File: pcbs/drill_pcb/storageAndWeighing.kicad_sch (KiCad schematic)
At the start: 34 parts, among them J401 Screw_Terminal_01x04, J402 Screw_Terminal_01x06, J403 Screw_Terminal_01x04, SW401 SW_Push, SW402 SW_Push, SW403 SW_Push, U401 HT75xx-1-SOT89

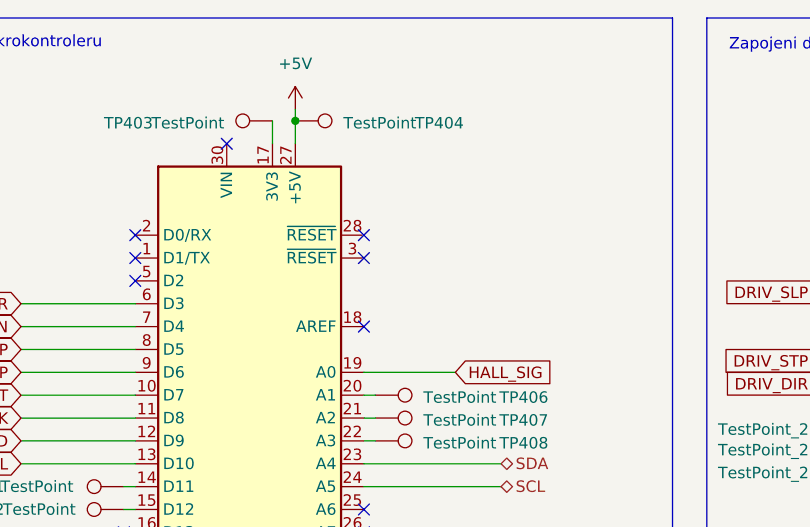
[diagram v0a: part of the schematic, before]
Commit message: added RESET connections into subsheets
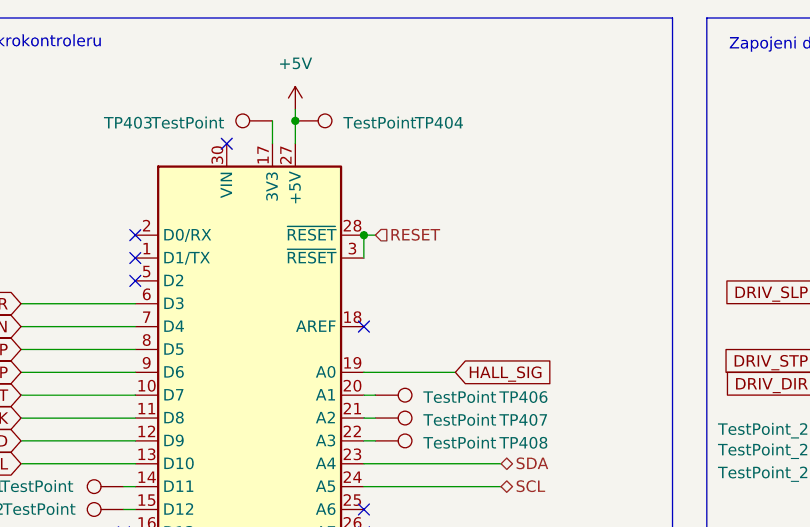
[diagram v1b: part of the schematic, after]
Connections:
- net RESET: now reaches A401.28 (~{RESET})
- net RESET: now also A401.3 (~{RESET})
- no-connect marks 11 -> 9
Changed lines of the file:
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@@
+	)
+	(junction
+		(at 68.58 39.37)
+		(diameter 0)
+		(color 0 0 0 0)
 	)
 	(junction
@@
 	)
 	(no_connect
-		(at 68.58 39.37)
-	)
-	(no_connect
 		(at 41.91 72.39)
 	)
@@
 	)
 	(no_connect
-		(at 68.58 41.91)
-	)
-	(no_connect
 		(at 68.58 72.39)
 	)
@@
 	(wire
 		(pts
+			(xy 68.58 39.37) (xy 69.85 39.37)
+		)
+		(stroke
+			(width 0)
+			(type default)
+		)
+	)
+	(wire
+		(pts
 			(xy 248.92 25.4) (xy 259.08 25.4)
 		)
@@
 		(pts
 			(xy 162.56 120.65) (xy 153.67 120.65)
+		)
+		(stroke
+			(width 0)
+			(type default)
+		)
+	)
+	(wire
+		(pts
+			(xy 68.58 39.37) (xy 68.58 41.91)
 		)
 		(stroke
@@
 		(fields_autoplaced yes)
 		(effects
+			(font
+				(size 1.27 1.27)
+			)
+			(justify left)
+		)
+	)
+	(hierarchical_label "RESET"
+		(shape input)
+		(at 69.85 39.37 0)
+		(fields_autoplaced yes)
+		(effects

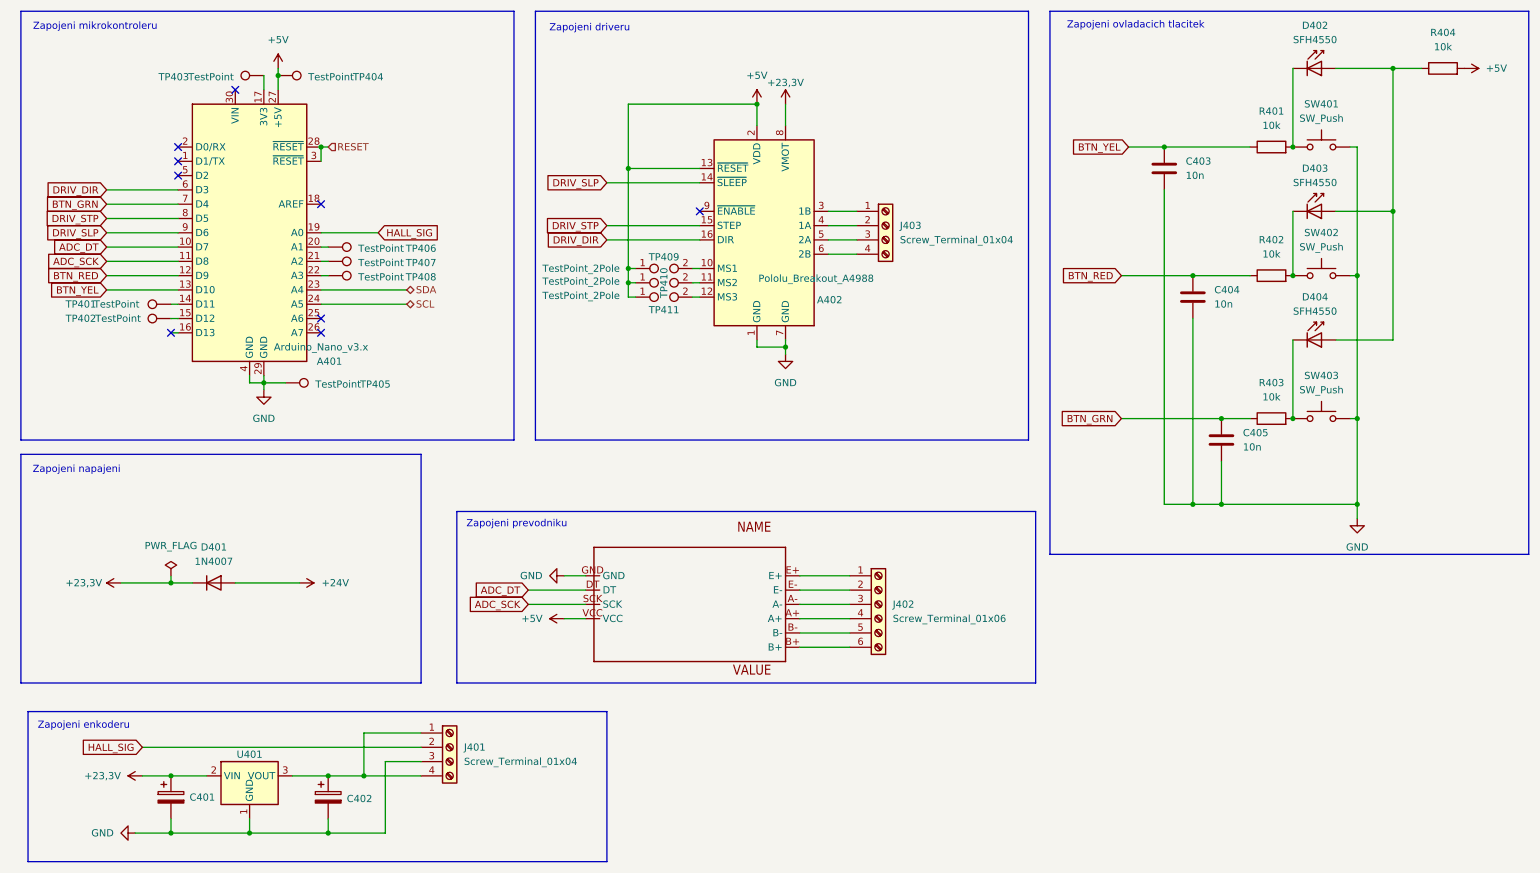
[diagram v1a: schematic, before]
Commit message: Mostly finished PCB v1.0.0 Missing strain gauge control circuit
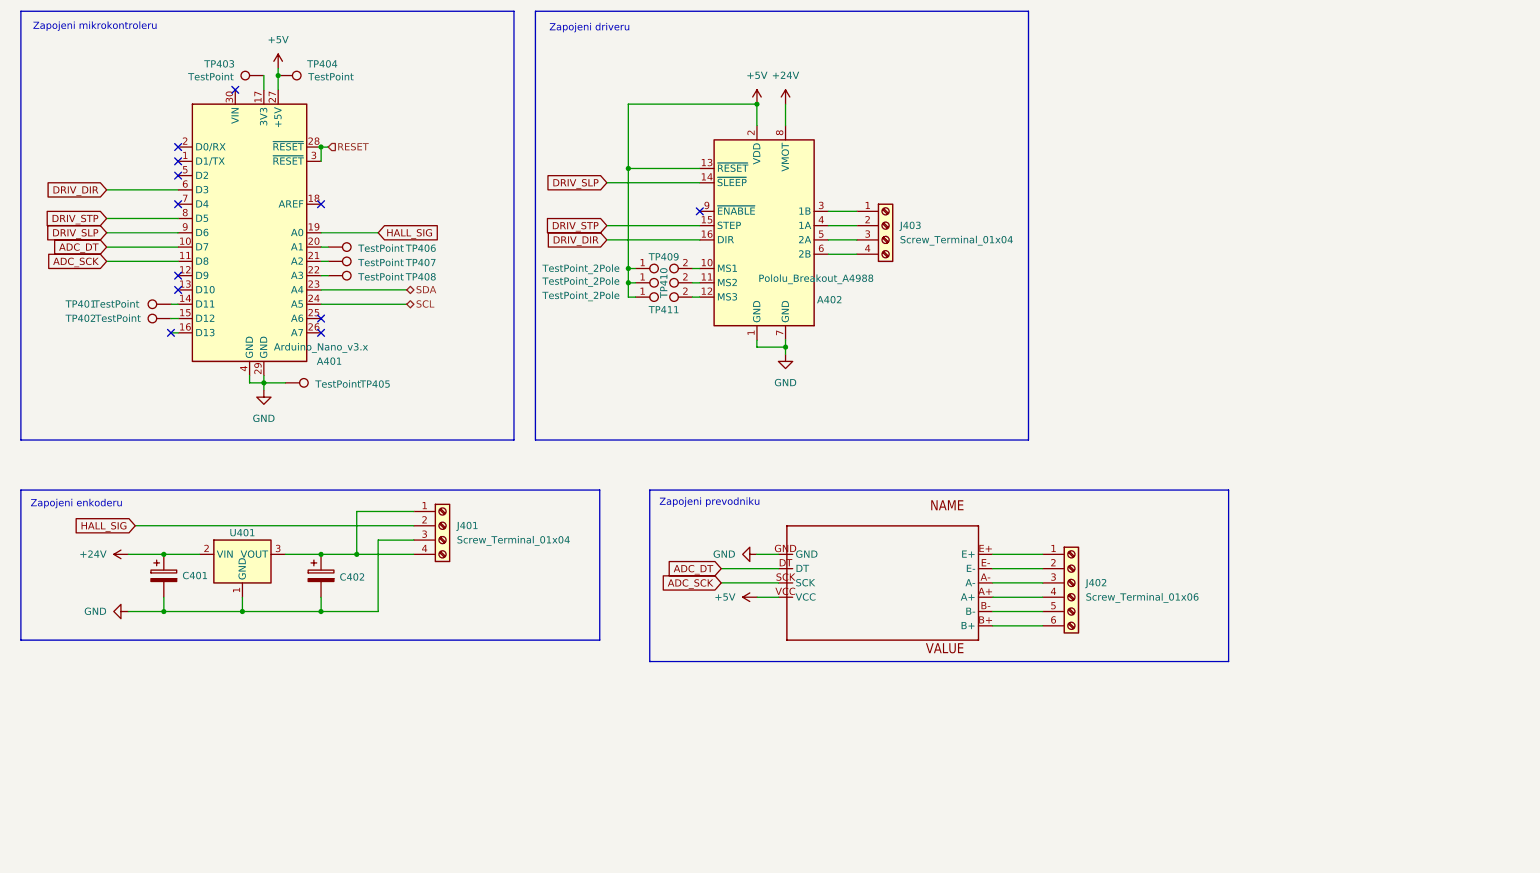
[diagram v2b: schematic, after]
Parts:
- removed C403, C404, C405: 10n, Capacitor_THT:C_Disc_D4.7mm_W2.5mm_P5.00mm, symbol Device:C
- removed D401: 1N4007, Diode_THT:D_DO-41_SOD81_P10.16mm_Horizontal, symbol Diode:1N4007
- removed D402, D403, D404: SFH4550, LED_THT:LED_D5.0mm_IRGrey, symbol LED:SFH4550
- removed R401, R402, R403, R404: 10k, Resistor_THT:R_Axial_DIN0207_L6.3mm_D2.5mm_P10.16mm_Horizontal, symbol Device:R
- removed SW401, SW402, SW403: SW_Push, Button_Switch_THT:SW_PUSH_6mm, symbol Switch:SW_Push
- J401, J403: footprint TerminalBlock_TE-Connectivity:TerminalBlock_TE_282834-4_1x04_P2.54mm_Horizontal -> Connector_JST:JST_XH_B4B-XH-A_1x04_P2.50mm_Vertical
- J402: footprint TerminalBlock_TE-Connectivity:TerminalBlock_TE_282834-6_1x06_P2.54mm_Horizontal -> Connector_JST:JST_XH_B6B-XH-A_1x06_P2.50mm_Vertical
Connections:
- net +23,3V is gone; now on net +24V: A402.8 (VMOT), C401.1, U401.2 (VIN)
- net BTN_GRN: no longer names the net of A401.7 (D4)
- net BTN_RED: no longer names the net of A401.12 (D9)
- net BTN_YEL: no longer names the net of A401.13 (D10)
- no-connect marks 9 -> 12
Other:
- note removed: "Zapojeni napajeni"
- note removed: "Zapojeni ovladacich tlacitek"
- moved on the sheet: C401, C402, J401, J402, U401

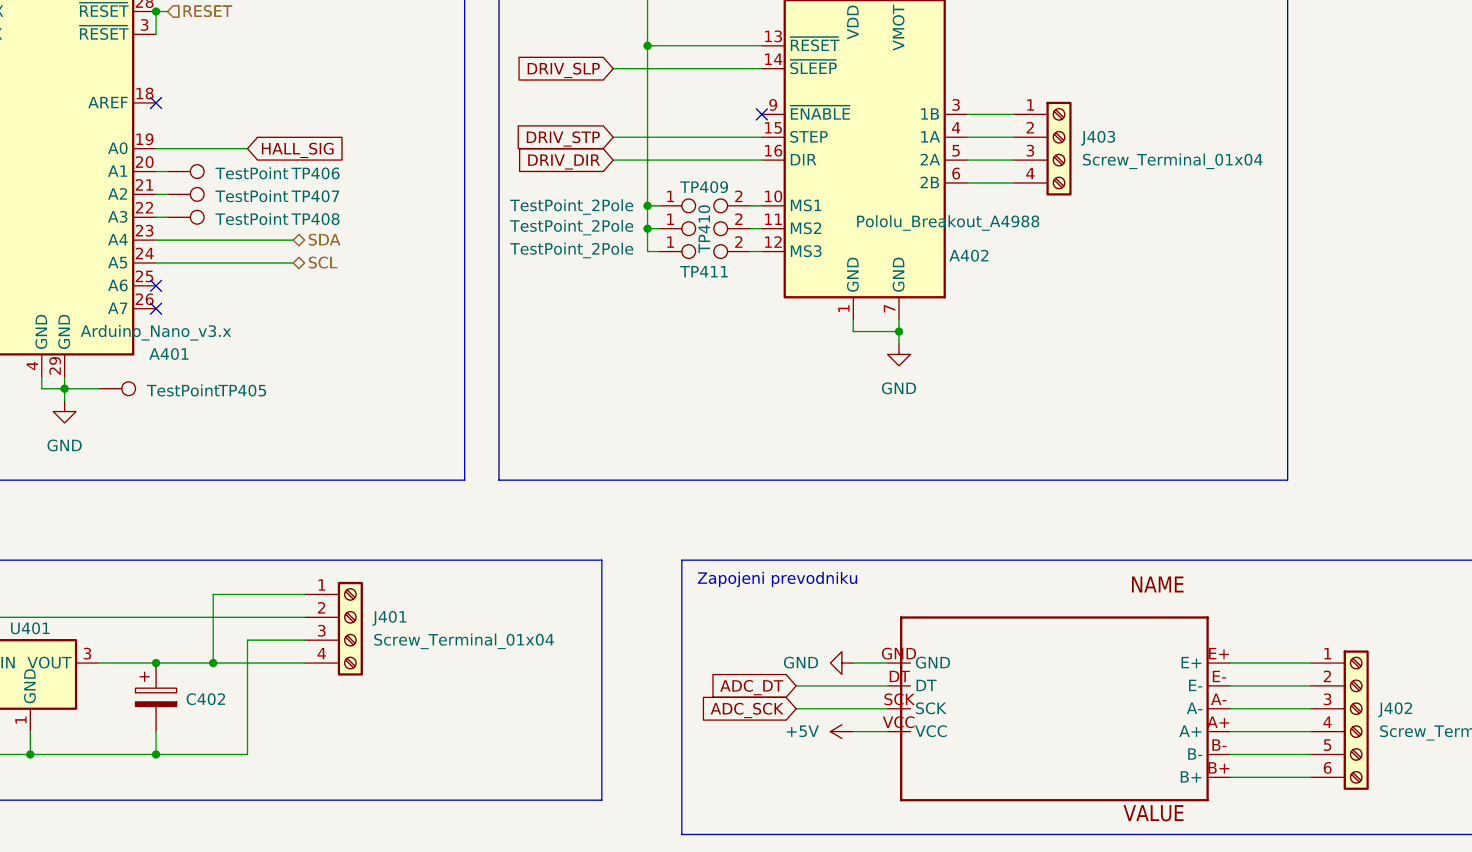
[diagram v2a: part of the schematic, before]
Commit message: update pouzdra konvertoru
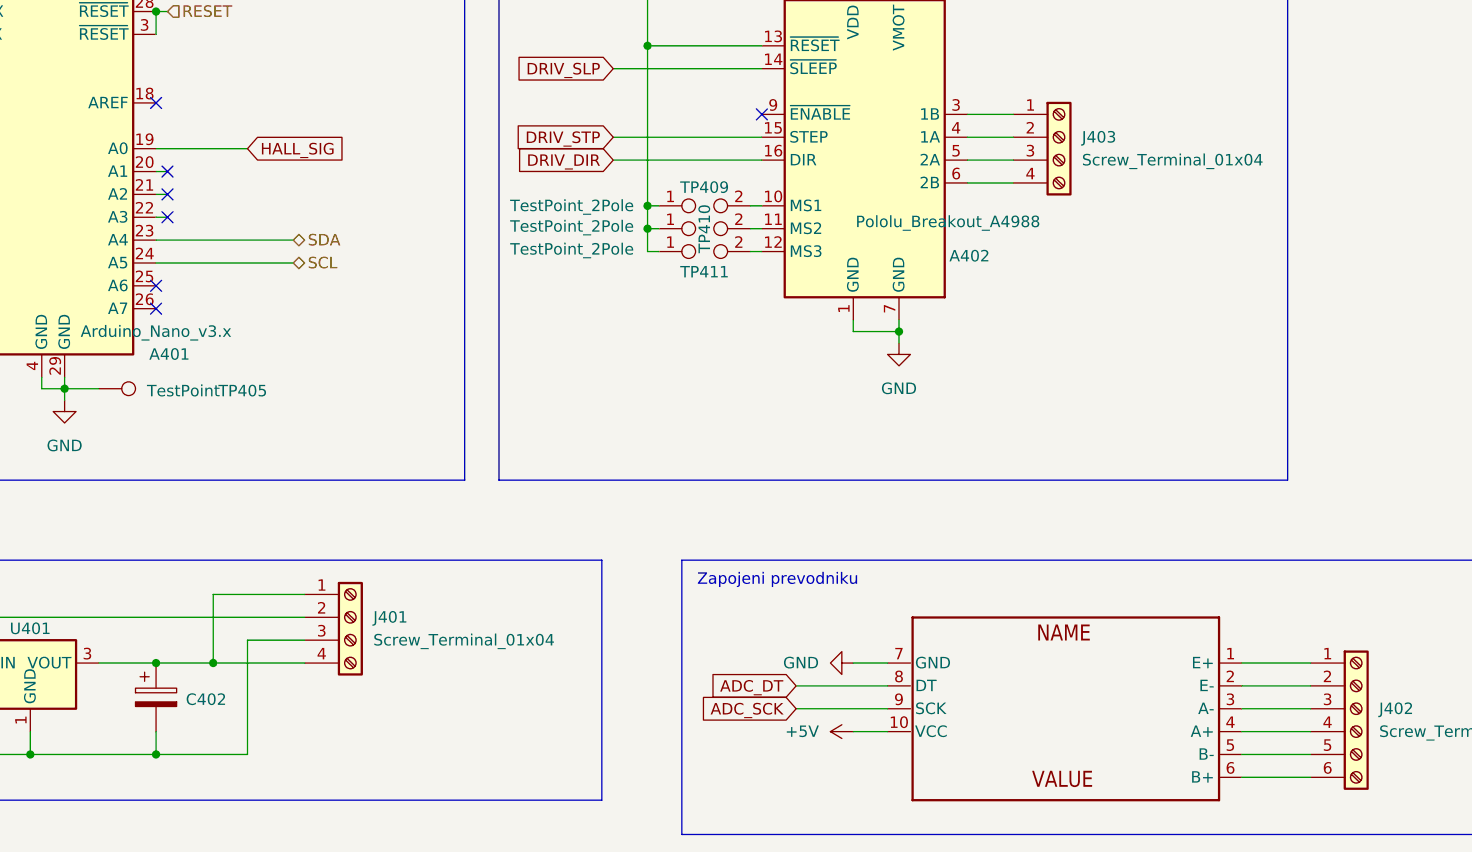
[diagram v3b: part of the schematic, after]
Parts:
- removed TP406, TP407, TP408: TestPoint, TestPoint:TestPoint_Pad_1.5x1.5mm, symbol Connector:TestPoint
- 1111401: footprint hx711footp:HX711 -> drill_hx711footp:HX711
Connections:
- net +5V: now also 1111401.10 (VCC); no longer 1111401.VCC
- net ADC_DT: now also 1111401.8 (DT); no longer 1111401.DT
- net ADC_SCK: now also 1111401.9 (SCK); no longer 1111401.SCK
- net GND: now also 1111401.7 (GND); no longer 1111401.GND
- net at J402.4 (Pin_4): now also 1111401.4 (A+); no longer 1111401.A+
- net at J402.3 (Pin_3): now also 1111401.3 (A-); no longer 1111401.A-
- net at J402.6 (Pin_6): now also 1111401.6 (B+); no longer 1111401.B+
- net at J402.5 (Pin_5): now also 1111401.5 (B-); no longer 1111401.B-
- net at J402.1 (Pin_1): now also 1111401.1 (E+); no longer 1111401.E+
- net at J402.2 (Pin_2): now also 1111401.2 (E-); no longer 1111401.E-
- no-connect marks 12 -> 15

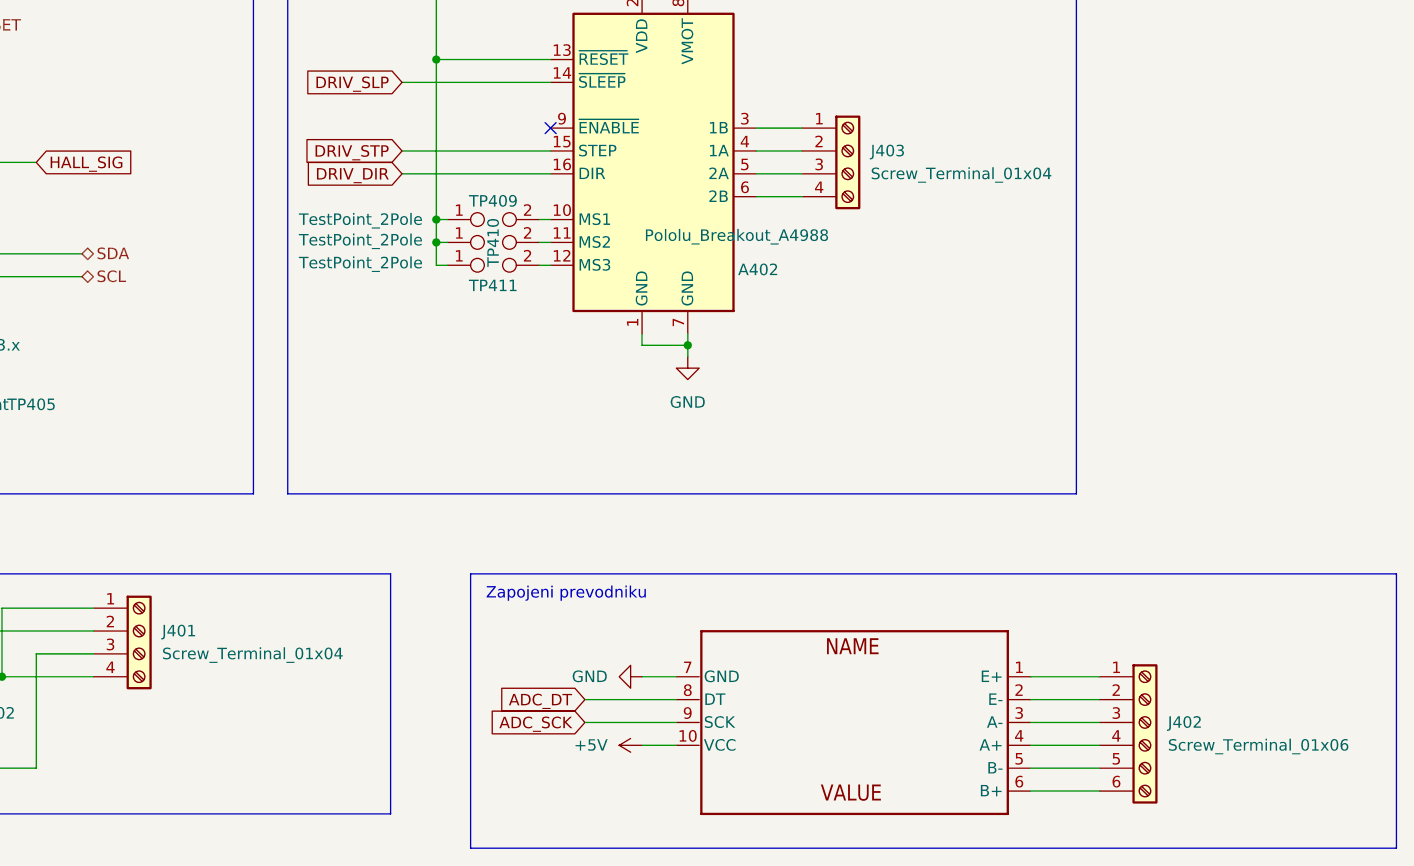
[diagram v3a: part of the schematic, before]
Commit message: PCB update Fixed connector silkscreen. Added H-bridge capacitors.
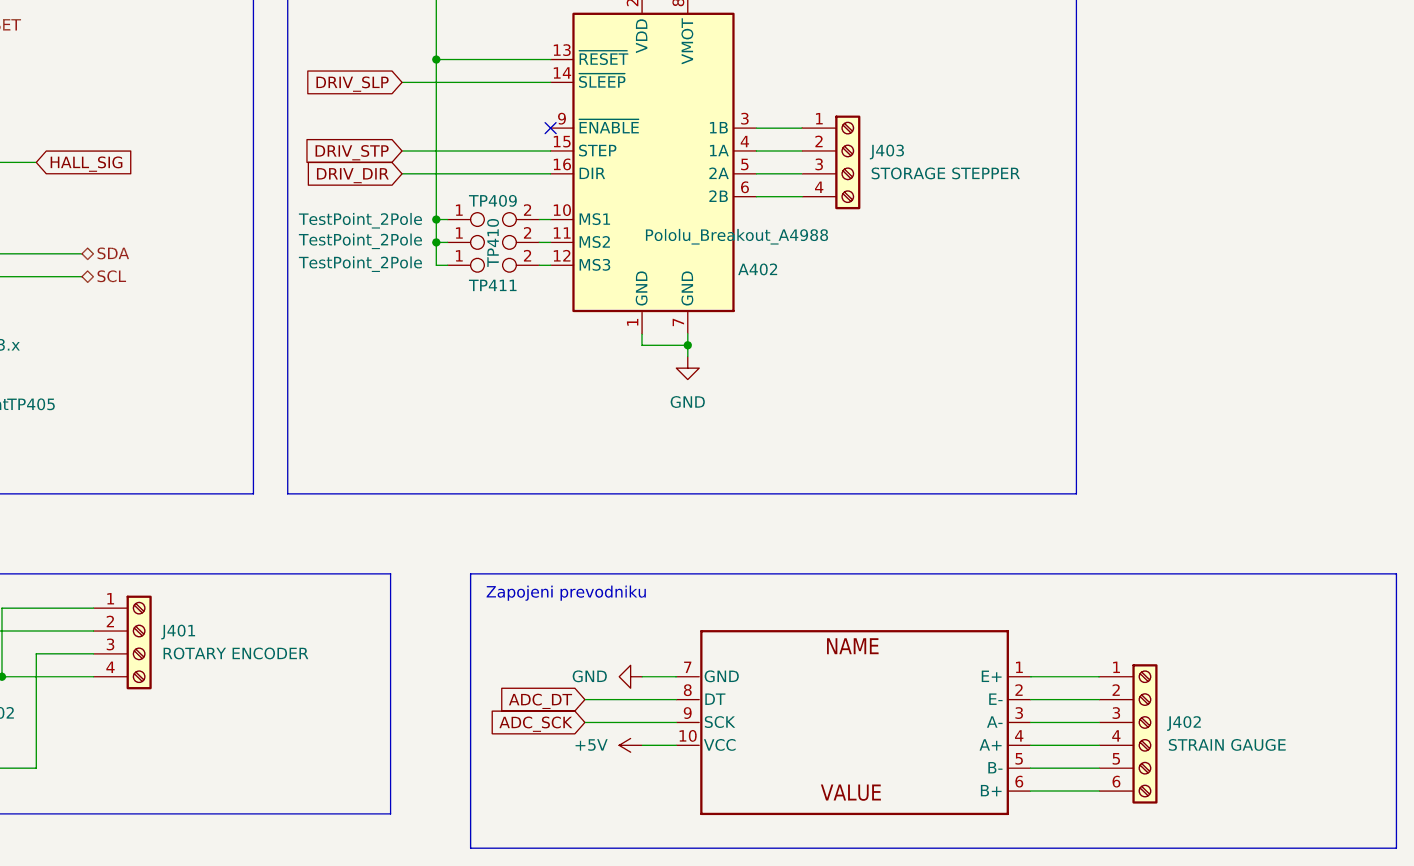
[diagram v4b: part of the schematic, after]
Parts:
- J401: value Screw_Terminal_01x04 -> ROTARY ENCODER
- J402: value Screw_Terminal_01x06 -> STRAIN GAUGE
- J403: value Screw_Terminal_01x04 -> STORAGE STEPPER
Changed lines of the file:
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@@
 			)
 		)
-		(property "Value" "Screw_Terminal_01x06"
+		(property "Value" "STRAIN GAUGE"
 			(at 204.47 119.3799 0)
 			(effects
@@
 			)
 		)
-		(property "Value" "Screw_Terminal_01x04"
+		(property "Value" "STORAGE STEPPER"
 			(at 171.45 55.8799 0)
 			(effects
@@
 			)
 		)
-		(property "Value" "Screw_Terminal_01x04"
+		(property "Value" "ROTARY ENCODER"
 			(at 92.71 109.2199 0)
 			(effects

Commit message: PCB update
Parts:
- C401, C402: value C_Polarized -> 10u
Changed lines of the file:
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@@
 			)
 		)
-		(property "Value" "C_Polarized"
-			(at 62.992 118.618 0)
+		(property "Value" "10u"
+			(at 72.136 118.11 0)
 			(effects
 				(font
@@
 				)
 				(justify left)
-				(hide yes)
 			)
 		)
@@
 			)
 		)
-		(property "Value" "C_Polarized"
-			(at 35.052 118.364 0)
+		(property "Value" "10u"
+			(at 44.196 117.856 0)
 			(effects
 				(font
@@
 				)
 				(justify left)
-				(hide yes)
-			)
-		)
+			)
+		)
